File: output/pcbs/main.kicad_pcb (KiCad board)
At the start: 2 copper layers, 227.6 x 75.2 mm, 143 parts

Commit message: Remove top-left key, move rotary encoder to top-left corner
- Remove matrix_one_top key (replaced by rotary encoder knob)
- Move rotary encoder from top-right to top-left corner
- Renumber LED chain: 46 -> 45 LEDs (LED_1 at matrix_one_home)
- Add bind: 5 to key defaults to bridge matrix/modrow gap
- Add circle outline at encoder position for knob shape
- Filter switches, diodes, and bounds to exclude matrix_one_top
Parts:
- removed D46: , ceoloide:diode_tht_sod123
- removed LED46: , ceoloide:led_SK6812mini-e (per-keysingle-side)
- removed S46: , MX
- moved D36 210.4 mm to (50.0, 90.5)
- moved S36 210.4 mm to (50.0, 100.0)
- moved RE1 209.6 mm to (50.0, 42.9)
- moved D18 42.6 mm to (164.3, 33.4)
- moved D24 42.6 mm to (202.4, 33.4)
- moved D30 42.6 mm to (240.5, 33.4)
- moved D33 42.6 mm to (259.6, 33.4)
- moved D9 42.6 mm to (107.2, 33.4)
- moved S18 42.6 mm to (164.3, 42.9)
- moved S24 42.6 mm to (202.4, 42.9)
- moved S30 42.6 mm to (240.5, 42.9)
- moved S33 42.6 mm to (259.6, 42.9)
- moved S9 42.6 mm to (107.2, 42.9)
- moved D12 42.6 mm to (126.2, 33.4)
- moved D15 42.6 mm to (145.2, 33.4)
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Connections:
- D1 pad 2: one_top -> one_home
- D10 pad 2: four_top -> four_home
- D11 pad 2: four_home -> four_bottom
- D12 pad 1: P20 -> P2
- D12 pad 2: four_bottom -> five_top
- D13 pad 2: five_top -> five_home
- D14 pad 2: five_home -> five_bottom
- D15 pad 1: P2 -> P3
- D15 pad 2: five_bottom -> six_top
- D16 pad 2: six_top -> six_home
- D17 pad 2: six_home -> six_bottom
- D18 pad 1: P3 -> P4
- D18 pad 2: six_bottom -> seven_top
- D19 pad 2: seven_top -> seven_home
- D2 pad 2: one_home -> one_bottom
- D20 pad 2: seven_home -> seven_bottom
- D21 pad 1: P4 -> P5
- D21 pad 2: seven_bottom -> eight_top
- D22 pad 2: eight_top -> eight_home
- D23 pad 2: eight_home -> eight_bottom
- D24 pad 1: P5 -> P6
- D24 pad 2: eight_bottom -> nine_top
- D25 pad 2: nine_top -> nine_home
- D26 pad 2: nine_home -> nine_bottom
- D27 pad 1: P6 -> P7
- D27 pad 2: nine_bottom -> ten_top
- D28 pad 2: ten_top -> ten_home
- D29 pad 2: ten_home -> ten_bottom
- D3 pad 1: P1 -> P0
- D3 pad 2: one_bottom -> two_top
- D30 pad 1: P7 -> P8
- D30 pad 2: ten_bottom -> eleven_top
- D31 pad 2: eleven_top -> eleven_home
- D32 pad 2: eleven_home -> eleven_bottom
- D33 pad 1: P8 -> P9
- D33 pad 2: eleven_bottom -> twelve_top
- D34 pad 2: twelve_top -> twelve_home
- D35 pad 2: twelve_home -> twelve_bottom
- D36 pad 1: P9 -> P1
- D36 pad 2: twelve_bottom -> one_mod
- D37 pad 1: P1 -> P0
- D37 pad 2: one_mod -> two_mod
- D38 pad 1: P0 -> P14
- D38 pad 2: two_mod -> three_mod
- D39 pad 1: P14 -> P20
- D39 pad 2: three_mod -> four_mod
- D4 pad 2: two_top -> two_home
- D40 pad 1: P20 -> P2
- D40 pad 2: four_mod -> five_mod
- D41 pad 1: P2 -> P5
- D41 pad 2: five_mod -> eight_mod
- D42 pad 1: P5 -> P6
- D42 pad 2: eight_mod -> nine_mod
- D43 pad 1: P6 -> P7
- D43 pad 2: nine_mod -> ten_mod
- D44 pad 1: P7 -> P8
- D44 pad 2: ten_mod -> eleven_mod
- D45 pad 1: P8 -> P9
- D45 pad 2: eleven_mod -> twelve_mod
- D5 pad 2: two_home -> two_bottom
- D6 pad 1: P0 -> P14
- D6 pad 2: two_bottom -> three_top
- D7 pad 2: three_top -> three_home
- D8 pad 2: three_home -> three_bottom
- D9 pad 1: P14 -> P20
- D9 pad 2: three_bottom -> four_top
- S1 pad 2: one_top -> one_home
- S10 pad 2: four_top -> four_home
- S11 pad 2: four_home -> four_bottom
- S12 pad 1: P20 -> P2
- S12 pad 2: four_bottom -> five_top
- S13 pad 2: five_top -> five_home
- S14 pad 2: five_home -> five_bottom
- S15 pad 1: P2 -> P3
- S15 pad 2: five_bottom -> six_top
- S16 pad 2: six_top -> six_home
- S17 pad 2: six_home -> six_bottom
- S18 pad 1: P3 -> P4
- S18 pad 2: six_bottom -> seven_top
- S19 pad 2: seven_top -> seven_home
- S2 pad 2: one_home -> one_bottom
- S20 pad 2: seven_home -> seven_bottom
- S21 pad 1: P4 -> P5
- S21 pad 2: seven_bottom -> eight_top
- S22 pad 2: eight_top -> eight_home
- S23 pad 2: eight_home -> eight_bottom
- S24 pad 1: P5 -> P6
- S24 pad 2: eight_bottom -> nine_top
- S25 pad 2: nine_top -> nine_home
- S26 pad 2: nine_home -> nine_bottom
- S27 pad 1: P6 -> P7
- S27 pad 2: nine_bottom -> ten_top
- S28 pad 2: ten_top -> ten_home
- S29 pad 2: ten_home -> ten_bottom
- S3 pad 1: P1 -> P0
- S3 pad 2: one_bottom -> two_top
- S30 pad 1: P7 -> P8
- S30 pad 2: ten_bottom -> eleven_top
- S31 pad 2: eleven_top -> eleven_home
- S32 pad 2: eleven_home -> eleven_bottom
- S33 pad 1: P8 -> P9
- S33 pad 2: eleven_bottom -> twelve_top
- S34 pad 2: twelve_top -> twelve_home
- S35 pad 2: twelve_home -> twelve_bottom
- S36 pad 1: P9 -> P1
- S36 pad 2: twelve_bottom -> one_mod
- S37 pad 1: P1 -> P0
- S37 pad 2: one_mod -> two_mod
- S38 pad 1: P0 -> P14
- S38 pad 2: two_mod -> three_mod
- S39 pad 1: P14 -> P20
- S39 pad 2: three_mod -> four_mod
- S4 pad 2: two_top -> two_home
- S40 pad 1: P20 -> P2
- S40 pad 2: four_mod -> five_mod
- S41 pad 1: P2 -> P5
- S41 pad 2: five_mod -> eight_mod
- S42 pad 1: P5 -> P6
- S42 pad 2: eight_mod -> nine_mod
- S43 pad 1: P6 -> P7
- S43 pad 2: nine_mod -> ten_mod
- S44 pad 1: P7 -> P8
- S44 pad 2: ten_mod -> eleven_mod
- S45 pad 1: P8 -> P9
- S45 pad 2: eleven_mod -> twelve_mod
- S5 pad 2: two_home -> two_bottom
- S6 pad 1: P0 -> P14
- S6 pad 2: two_bottom -> three_top
- S7 pad 2: three_top -> three_home
- S8 pad 2: three_home -> three_bottom
- S9 pad 1: P14 -> P20
- S9 pad 2: three_bottom -> four_top
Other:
- board size 227.6 x 75.2 mm -> 242.6 x 90.2 mm

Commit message: Move rotary encoder to top-right, tighten outline
- Move rotary encoder from top-left to top-right corner
- Remove matrix_twelve_top key (replaced by knob)
- Restore matrix_one_top key
- Tighten outline: 18.5mm key bounds, bind=3 for slim profile
- Knob circle at top-right with 9.25mm radius + 2.5mm expand
- 45 switches, 45 diodes, 45 LEDs, 1 rotary encoder
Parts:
- moved RE1 209.6 mm to (259.6, 42.9)
- moved D18 42.6 mm to (145.2, 71.5)
- moved D24 42.6 mm to (183.3, 71.5)
- moved D30 42.6 mm to (221.4, 71.5)
- moved D33 42.6 mm to (240.5, 71.5)
- moved D9 42.6 mm to (88.1, 71.5)
- moved S18 42.6 mm to (145.2, 81.0)
- moved S24 42.6 mm to (183.3, 81.0)
- moved S30 42.6 mm to (221.4, 81.0)
- moved S33 42.6 mm to (240.5, 81.0)
- moved S9 42.6 mm to (88.1, 81.0)
- moved D12 42.6 mm to (107.2, 71.5)
- moved D15 42.6 mm to (126.2, 71.5)
- moved D3 42.6 mm to (50.0, 71.5)
- moved D6 42.6 mm to (69.0, 71.5)
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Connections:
- D1 pad 2: one_home -> one_top
- D10 pad 2: four_home -> four_top
- D11 pad 2: four_bottom -> four_home
- D12 pad 1: P2 -> P20
- D12 pad 2: five_top -> four_bottom
- D13 pad 2: five_home -> five_top
- D14 pad 2: five_bottom -> five_home
- D15 pad 1: P3 -> P2
- D15 pad 2: six_top -> five_bottom
- D16 pad 2: six_home -> six_top
- D17 pad 2: six_bottom -> six_home
- D18 pad 1: P4 -> P3
- D18 pad 2: seven_top -> six_bottom
- D19 pad 2: seven_home -> seven_top
- D2 pad 2: one_bottom -> one_home
- D20 pad 2: seven_bottom -> seven_home
- D21 pad 1: P5 -> P4
- D21 pad 2: eight_top -> seven_bottom
- D22 pad 2: eight_home -> eight_top
- D23 pad 2: eight_bottom -> eight_home
- D24 pad 1: P6 -> P5
- D24 pad 2: nine_top -> eight_bottom
- D25 pad 2: nine_home -> nine_top
- D26 pad 2: nine_bottom -> nine_home
- D27 pad 1: P7 -> P6
- D27 pad 2: ten_top -> nine_bottom
- D28 pad 2: ten_home -> ten_top
- D29 pad 2: ten_bottom -> ten_home
- D3 pad 1: P0 -> P1
- D3 pad 2: two_top -> one_bottom
- D30 pad 1: P8 -> P7
- D30 pad 2: eleven_top -> ten_bottom
- D31 pad 2: eleven_home -> eleven_top
- D32 pad 2: eleven_bottom -> eleven_home
- D33 pad 1: P9 -> P8
- D33 pad 2: twelve_top -> eleven_bottom
- D4 pad 2: two_home -> two_top
- D5 pad 2: two_bottom -> two_home
- D6 pad 1: P14 -> P0
- D6 pad 2: three_top -> two_bottom
- D7 pad 2: three_home -> three_top
- D8 pad 2: three_bottom -> three_home
- D9 pad 1: P20 -> P14
- D9 pad 2: four_top -> three_bottom
- S1 pad 2: one_home -> one_top
- S10 pad 2: four_home -> four_top
- S11 pad 2: four_bottom -> four_home
- S12 pad 1: P2 -> P20
- S12 pad 2: five_top -> four_bottom
- S13 pad 2: five_home -> five_top
- S14 pad 2: five_bottom -> five_home
- S15 pad 1: P3 -> P2
- S15 pad 2: six_top -> five_bottom
- S16 pad 2: six_home -> six_top
- S17 pad 2: six_bottom -> six_home
- S18 pad 1: P4 -> P3
- S18 pad 2: seven_top -> six_bottom
- S19 pad 2: seven_home -> seven_top
- S2 pad 2: one_bottom -> one_home
- S20 pad 2: seven_bottom -> seven_home
- S21 pad 1: P5 -> P4
- S21 pad 2: eight_top -> seven_bottom
- S22 pad 2: eight_home -> eight_top
- S23 pad 2: eight_bottom -> eight_home
- S24 pad 1: P6 -> P5
- S24 pad 2: nine_top -> eight_bottom
- S25 pad 2: nine_home -> nine_top
- S26 pad 2: nine_bottom -> nine_home
- S27 pad 1: P7 -> P6
- S27 pad 2: ten_top -> nine_bottom
- S28 pad 2: ten_home -> ten_top
- S29 pad 2: ten_bottom -> ten_home
- S3 pad 1: P0 -> P1
- S3 pad 2: two_top -> one_bottom
- S30 pad 1: P8 -> P7
- S30 pad 2: eleven_top -> ten_bottom
- S31 pad 2: eleven_home -> eleven_top
- S32 pad 2: eleven_bottom -> eleven_home
- S33 pad 1: P9 -> P8
- S33 pad 2: twelve_top -> eleven_bottom
- S4 pad 2: two_home -> two_top
- S5 pad 2: two_bottom -> two_home
- S6 pad 1: P14 -> P0
- S6 pad 2: three_top -> two_bottom
- S7 pad 2: three_home -> three_top
- S8 pad 2: three_bottom -> three_home
- S9 pad 1: P20 -> P14
- S9 pad 2: four_top -> three_bottom
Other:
- board size 242.6 x 90.2 mm -> 239.1 x 86.7 mm

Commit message: Tighten outline to follow keycap edges
- Remove bind to eliminate extra outline padding
- Use 18.5mm key bounds (matching keycap width)
- Knob circle at top-right with 9.25mm radius + 2.5mm expand
- Outline: 233x81mm, ~11.75mm uniform margins
- Single continuous outline, no gaps
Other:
- board size 239.1 x 86.7 mm -> 233.1 x 80.7 mm
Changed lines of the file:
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@@
         (pad "2" thru_hole oval (at 1 0 90) (size 1.2 1.75) (drill 0.75) (layers "*.Cu" "*.Mask") (net 143 "BAT_P"))
     )
-  (gr_line (start 37.75 28.1) (end 252.75 28.1) (layer Edge.Cuts) (stroke (width 0.15) (type default)))
-(gr_arc (start 255.25 30.6) (mid 254.517767 28.832233000000002) (end 252.75 28.1) (layer Edge.Cuts) (stroke (width 0.15) (type default)))
-(gr_line (start 255.25 31.915078900000008) (end 255.25 30.600000000000005) (layer Edge.Cuts) (stroke (width 0.15) (type default)))
-(gr_arc (start 270.4849211 47.150000000000006) (mid 267.8585047 34.54149530000001) (end 255.25 31.915078900000008) (layer Edge.Cuts) (stroke (width 0.15) (type default)))
-(gr_line (start 270.4849211 47.150000000000006) (end 271.8 47.150000000000006) (layer Edge.Cuts) (stroke (width 0.15) (type default)))
-(gr_arc (start 274.3 49.650000000000006) (mid 273.567767 47.88223300000001) (end 271.8 47.150000000000006) (layer Edge.Cuts) (stroke (width 0.15) (type default)))
-(gr_line (start 274.3 112.25) (end 274.3 49.65) (layer Edge.Cuts) (stroke (width 0.15) (type default)))
-(gr_arc (start 271.8 114.75) (mid 273.567767 114.017767) (end 274.3 112.25) (layer Edge.Cuts) (stroke (width 0.15) (type default)))
-(gr_line (start 190.15 114.75) (end 271.8 114.75) (layer Edge.Cuts) (stroke (width 0.15) (type default)))
-(gr_arc (start 188.1125 113.6986524) (mid 189.0036211 114.4716695) (end 190.15 114.75) (layer Edge.Cuts) (stroke (width 0.15) (type default)))
-(gr_arc (start 186.075 114.75) (mid 187.2213789 114.4716695) (end 188.11249999999998 113.6986524) (layer Edge.Cuts) (stroke (width 0.15) (type default)))
-(gr_line (start 161.575 114.75) (end 186.075 114.75) (layer Edge.Cuts) (stroke (width 0.15) (type default)))
-(gr_arc (start 159.5375 113.6986524) (mid 160.4286211 114.4716695) (end 161.575 114.75) (layer Edge.Cuts) (stroke (width 0.15) (type default)))
-(gr_arc (start 157.5 114.75) (mid 158.6463789 114.4716695) (end 159.5375 113.6986524) (layer Edge.Cuts) (stroke (width 0.15) (type default)))
-(gr_line (start 133 114.75) (end 157.5 114.75) (layer Edge.Cuts) (stroke (width 0.15) (type default)))
-(gr_arc (start 130.9625 113.6986524) (mid 131.8536211 114.4716695) (end 133 114.75) (layer Edge.Cuts) (stroke (width 0.15) (type default)))
-(gr_arc (start 128.925 114.75) (mid 130.0713789 114.4716695) (end 130.9625 113.6986524) (layer Edge.Cuts) (stroke (width 0.15) (type default)))
-(gr_line (start 104.425 114.75) (end 128.925 114.75) (layer Edge.Cuts) (stroke (width 0.15) (type default)))
-(gr_arc (start 102.3875 113.6986524) (mid 103.2786211 114.4716695) (end 104.425 114.75) (layer Edge.Cuts) (stroke (width 0.15) (type default)))
-(gr_arc (start 100.35 114.75) (mid 101.4963789 114.4716695) (end 102.38749999999999 113.6986524) (layer Edge.Cuts) (stroke (width 0.15) (type default)))
-(gr_line (start 37.75 114.75) (end 100.35 114.75) (layer Edge.Cuts) (stroke (width 0.15) (type default)))
-(gr_arc (start 35.25 112.25) (mid 35.982233 114.017767) (end 37.75 114.75) (layer Edge.Cuts) (stroke (width 0.15) (type default)))
-(gr_line (start 35.25 112.25) (end 35.25 30.599999999999994) (layer Edge.Cuts) (stroke (width 0.15) (type default)))
-(gr_arc (start 37.75 28.1) (mid 35.982233 28.832233000000002) (end 35.25 30.6) (layer Edge.Cuts) (stroke (width 0.15) (type default)))
+  (gr_line (start 40.75 31.1) (end 259.75 31.1) (layer Edge.Cuts) (stroke (width 0.15) (type default)))
+(gr_arc (start 259.9210935 31.10586150000001) (mid 259.8355969 31.101465800000007) (end 259.75 31.10000000000001) (layer Edge.Cuts) (stroke (width 0.15) (type default)))
+(gr_arc (start 271.29413850000003 42.47890650000001) (mid 267.8585047 34.54149530000001) (end 259.9210935 31.10586150000001) (layer Edge.Cuts) (stroke (width 0.15) (type default)))
+(gr_arc (start 271.3 42.650000000000006) (mid 271.2985342 42.56440310000001) (end 271.29413850000003 42.47890650000001) (layer Edge.Cuts) (stroke (width 0.15) (type default)))
+(gr_line (start 271.3 90.2) (end 271.3 42.650000000000006) (layer Edge.Cuts) (stroke (width 0.15) (type default)))
+(gr_arc (start 271.284829 90.47500000000001) (mid 271.2962044 90.3377091) (end 271.3 90.2) (layer Edge.Cuts) (stroke (width 0.15) (type default)))
+(gr_arc (start 271.3 90.75) (mid 271.2962044 90.6122909) (end 271.284829 90.475) (layer Edge.Cuts) (stroke (width 0.15) (type default)))
+(gr_line (start 271.3 109.25) (end 271.3 90.75) (layer Edge.Cuts) (stroke (width 0.15) (type default)))
+(gr_arc (start 268.8 111.75) (mid 270.567767 111.017767) (end 271.3 109.25) (layer Edge.Cuts) (stroke (width 0.15) (type default)))
+(gr_line (start 40.75 111.75) (end 268.8 111.75) (layer Edge.Cuts) (stroke (width 0.15) (type default)))
+(gr_arc (start 38.25 109.25) (mid 38.982233 111.017767) (end 40.75 111.75) (layer Edge.Cuts) (stroke (width 0.15) (type default)))
+(gr_line (start 38.25 90.75) (end 38.25 109.25) (layer Edge.Cuts) (stroke (width 0.15) (type default)))
+(gr_arc (start 38.265171 90.475) (mid 38.253795600000004 90.6122909) (end 38.25 90.75) (layer Edge.Cuts) (stroke (width 0.15) (type default)))
+(gr_arc (start 38.25 90.2) (mid 38.253795600000004 90.3377091) (end 38.265171 90.47500000000001) (layer Edge.Cuts) (stroke (width 0.15) (type default)))
+(gr_line (start 38.25 90.2) (end 38.25 33.6) (layer Edge.Cuts) (stroke (width 0.15) (type default)))
+(gr_arc (start 40.75 31.1) (mid 38.982233 31.832233000000002) (end 38.25 33.6) (layer Edge.Cuts) (stroke (width 0.15) (type default)))
 )

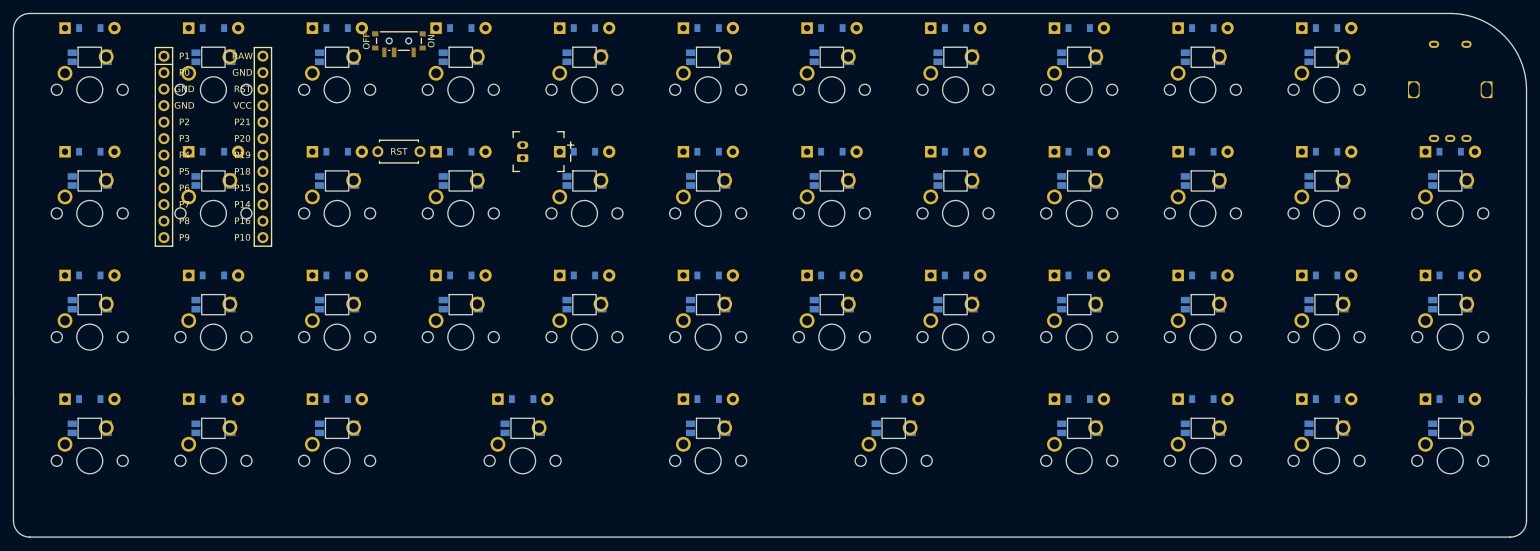
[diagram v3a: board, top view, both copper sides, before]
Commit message: Tight outline at keycap edges (228x76mm, 9.25mm margins)
- Single rectangle outline at exact keycap dimensions
- 9.25mm uniform margins (half of 18.5mm keycap)
- Knob circle at top-right with 9.25mm radius
- Minor: 0.5mm gap between matrix/modrow zones (fix in KiCad)
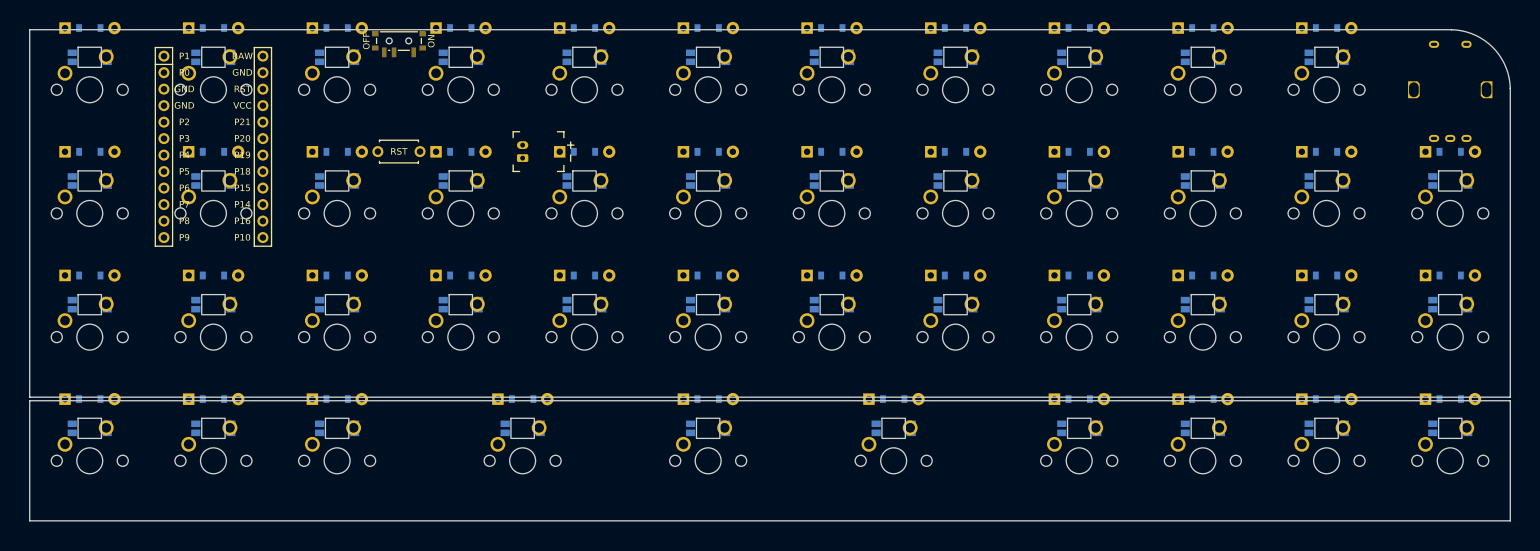
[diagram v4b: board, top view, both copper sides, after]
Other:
- board size 233.1 x 80.7 mm -> 228.1 x 75.7 mm
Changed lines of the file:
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@@
         (pad "2" thru_hole oval (at 1 0 90) (size 1.2 1.75) (drill 0.75) (layers "*.Cu" "*.Mask") (net 143 "BAT_P"))
     )
-  (gr_line (start 40.75 31.1) (end 259.75 31.1) (layer Edge.Cuts) (stroke (width 0.15) (type default)))
-(gr_arc (start 259.9210935 31.10586150000001) (mid 259.8355969 31.101465800000007) (end 259.75 31.10000000000001) (layer Edge.Cuts) (stroke (width 0.15) (type default)))
-(gr_arc (start 271.29413850000003 42.47890650000001) (mid 267.8585047 34.54149530000001) (end 259.9210935 31.10586150000001) (layer Edge.Cuts) (stroke (width 0.15) (type default)))
-(gr_arc (start 271.3 42.650000000000006) (mid 271.2985342 42.56440310000001) (end 271.29413850000003 42.47890650000001) (layer Edge.Cuts) (stroke (width 0.15) (type default)))
-(gr_line (start 271.3 90.2) (end 271.3 42.650000000000006) (layer Edge.Cuts) (stroke (width 0.15) (type default)))
-(gr_arc (start 271.284829 90.47500000000001) (mid 271.2962044 90.3377091) (end 271.3 90.2) (layer Edge.Cuts) (stroke (width 0.15) (type default)))
-(gr_arc (start 271.3 90.75) (mid 271.2962044 90.6122909) (end 271.284829 90.475) (layer Edge.Cuts) (stroke (width 0.15) (type default)))
-(gr_line (start 271.3 109.25) (end 271.3 90.75) (layer Edge.Cuts) (stroke (width 0.15) (type default)))
-(gr_arc (start 268.8 111.75) (mid 270.567767 111.017767) (end 271.3 109.25) (layer Edge.Cuts) (stroke (width 0.15) (type default)))
-(gr_line (start 40.75 111.75) (end 268.8 111.75) (layer Edge.Cuts) (stroke (width 0.15) (type default)))
-(gr_arc (start 38.25 109.25) (mid 38.982233 111.017767) (end 40.75 111.75) (layer Edge.Cuts) (stroke (width 0.15) (type default)))
-(gr_line (start 38.25 90.75) (end 38.25 109.25) (layer Edge.Cuts) (stroke (width 0.15) (type default)))
-(gr_arc (start 38.265171 90.475) (mid 38.253795600000004 90.6122909) (end 38.25 90.75) (layer Edge.Cuts) (stroke (width 0.15) (type default)))
-(gr_arc (start 38.25 90.2) (mid 38.253795600000004 90.3377091) (end 38.265171 90.47500000000001) (layer Edge.Cuts) (stroke (width 0.15) (type default)))
-(gr_line (start 38.25 90.2) (end 38.25 33.6) (layer Edge.Cuts) (stroke (width 0.15) (type default)))
-(gr_arc (start 40.75 31.1) (mid 38.982233 31.832233000000002) (end 38.25 33.6) (layer Edge.Cuts) (stroke (width 0.15) (type default)))
+  (gr_line (start 40.75 33.6) (end 259.75 33.60000000000001) (layer Edge.Cuts) (stroke (width 0.15) (type default)))
+(gr_line (start 40.75 90.2) (end 40.75 33.6) (layer Edge.Cuts) (stroke (width 0.15) (type default)))
+(gr_line (start 40.75 90.2) (end 268.8 90.2) (layer Edge.Cuts) (stroke (width 0.15) (type default)))
+(gr_line (start 259.75 33.6) (end 259.75 33.60216240000001) (layer Edge.Cuts) (stroke (width 0.15) (type default)))
+(gr_line (start 268.8 90.2) (end 268.8 42.650000000000006) (layer Edge.Cuts) (stroke (width 0.15) (type default)))
+(gr_line (start 268.79783760000004 42.650000000000006) (end 268.8 42.650000000000006) (layer Edge.Cuts) (stroke (width 0.15) (type default)))
+(gr_line (start 40.75 109.25) (end 268.8 109.25) (layer Edge.Cuts) (stroke (width 0.15) (type default)))
+(gr_line (start 40.75 90.75) (end 268.8 90.75) (layer Edge.Cuts) (stroke (width 0.15) (type default)))
+(gr_line (start 40.75 90.75) (end 40.75 109.25) (layer Edge.Cuts) (stroke (width 0.15) (type default)))
+(gr_line (start 268.8 109.25) (end 268.8 90.75) (layer Edge.Cuts) (stroke (width 0.15) (type default)))
+(gr_arc (start 268.79783760000004 42.650000000000006) (mid 266.09073770000003 36.30926230000001) (end 259.75 33.60216240000001) (layer Edge.Cuts) (stroke (width 0.15) (type default)))
 )
